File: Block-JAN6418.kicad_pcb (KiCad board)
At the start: 2 copper layers, 48 x 63 mm, 23 parts, among them U1 JAN6418, U2 LM317L

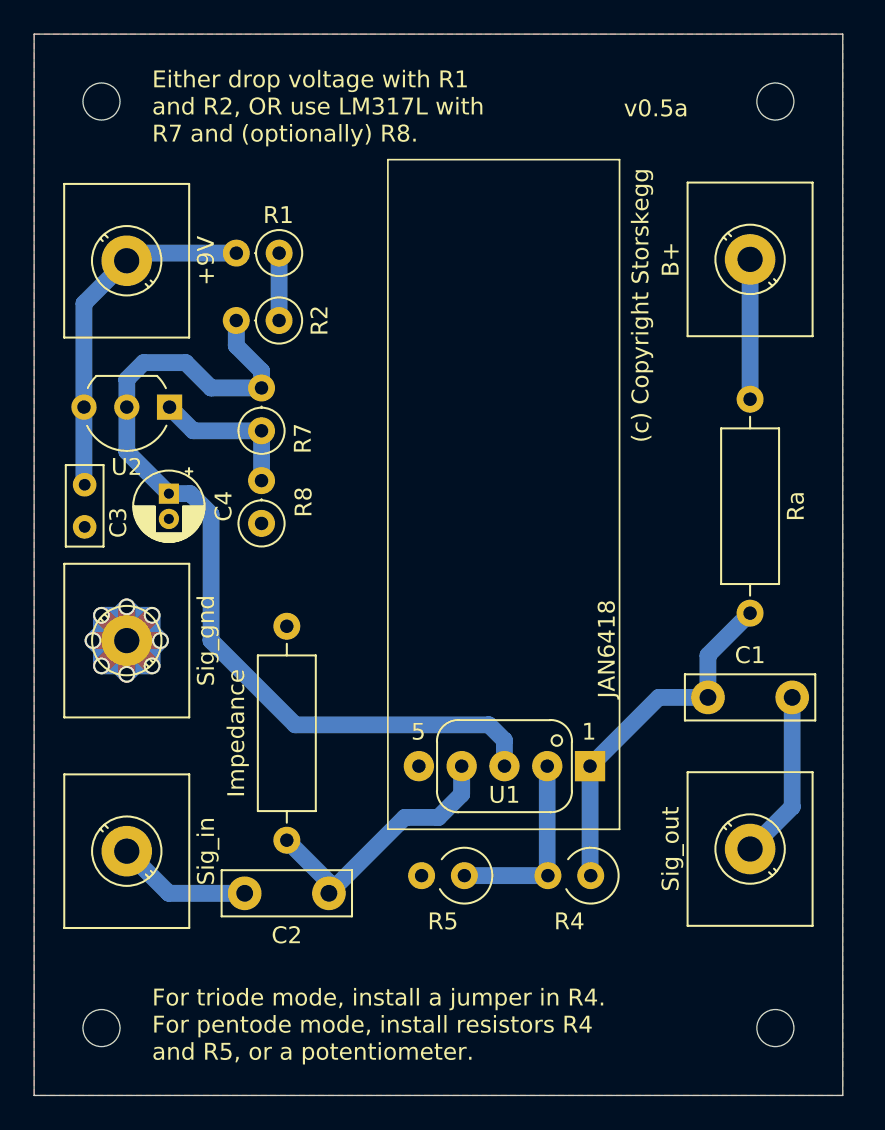
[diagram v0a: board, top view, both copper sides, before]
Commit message: v1.0b Re-routing
- Added ground fill to L2, respective vias
- Re-routed power rail solder points to the bottom of the board so that
  power can be jumpered up from the enclosure front board (will house
  power bars, I/O, pots, etc)
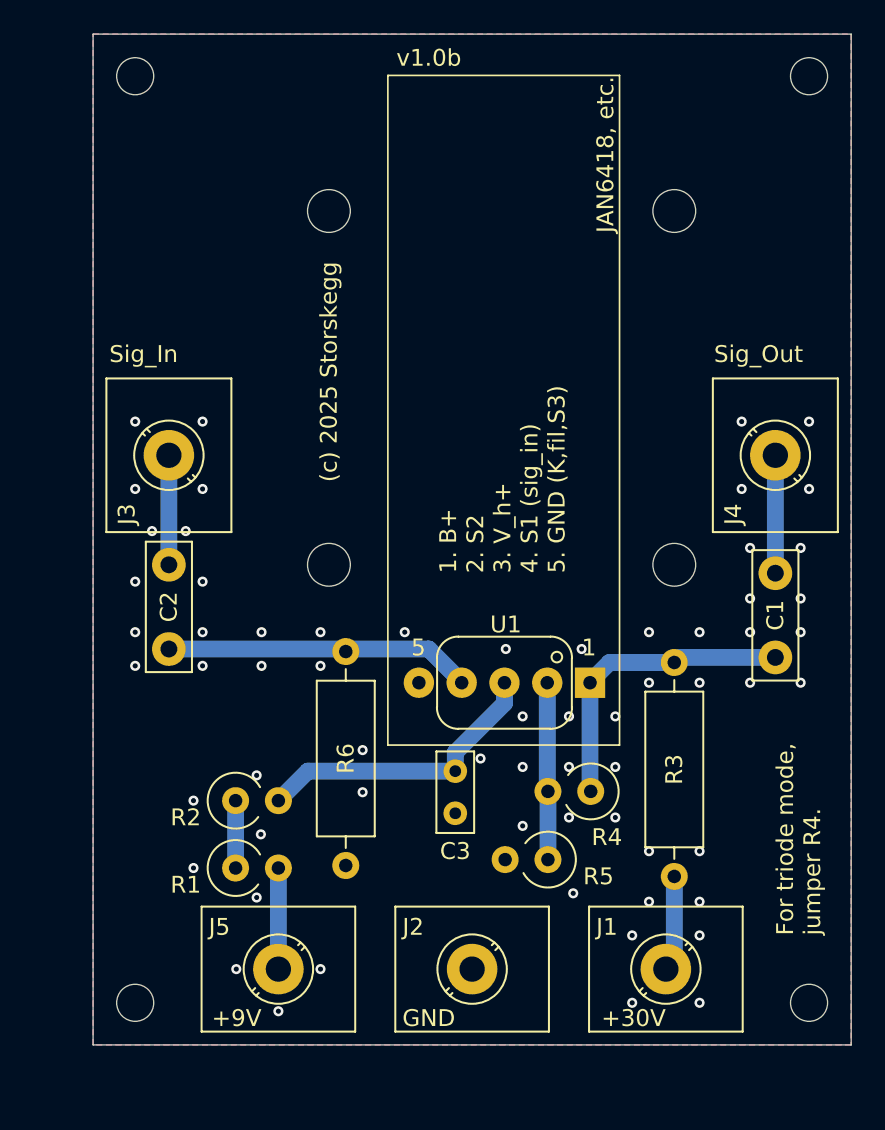
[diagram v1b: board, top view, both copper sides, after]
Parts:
- removed +9V: 9V, TerminalBlock_MetzConnect:TerminalBlock_MetzConnect_360271_1x01_Horizontal_ScrewM3.0_Boxed
- removed B+: B+, TerminalBlock_MetzConnect:TerminalBlock_MetzConnect_360271_1x01_Horizontal_ScrewM3.0_Boxed
- removed C4: 1uF, Capacitor_THT:CP_Radial_D4.0mm_P1.50mm
- removed Impedance: 1M, Resistor_THT:R_Axial_DIN0309_L9.0mm_D3.2mm_P12.70mm_Horizontal
- removed R7: R_r1, Resistor_THT:R_Axial_DIN0207_L6.3mm_D2.5mm_P2.54mm_Vertical
- removed R8: R_r2, Resistor_THT:R_Axial_DIN0207_L6.3mm_D2.5mm_P2.54mm_Vertical
- removed REF** (x4): MountingHole_2.2mm_M2, MountingHole:MountingHole_2.2mm_M2
- removed Ra: Ra, Resistor_THT:R_Axial_DIN0309_L9.0mm_D3.2mm_P12.70mm_Horizontal
- removed Sig_gnd: Sig_gnd, TerminalBlock_MetzConnect:TerminalBlock_MetzConnect_360271_1x01_Horizontal_ScrewM3.0_Boxed
- removed Sig_in: Sig_in, TerminalBlock_MetzConnect:TerminalBlock_MetzConnect_360271_1x01_Horizontal_ScrewM3.0_Boxed
- removed Sig_out: Sig_out, TerminalBlock_MetzConnect:TerminalBlock_MetzConnect_360271_1x01_Horizontal_ScrewM3.0_Boxed
- removed U2: LM317L, Package_TO_SOT_THT:TO-92_Inline_Wide
- added H1: MountingHole, MountingHole:MountingHole_2.2mm_M2, F.Cu at (56.0, 37.5)
- added H2: MountingHole, MountingHole:MountingHole_2.2mm_M2, F.Cu at (96.0, 37.5)
- added H3: MountingHole, MountingHole:MountingHole_2.2mm_M2, F.Cu at (96.0, 92.5)
- added H4: MountingHole, MountingHole:MountingHole_2.2mm_M2, F.Cu at (56.0, 92.5)
- added J1: B+, TerminalBlock_MetzConnect:TerminalBlock_MetzConnect_360271_1x01_Horizontal_ScrewM3.0_Boxed, F.Cu at (87.5, 90.5)
- added J2: Sig_gnd, TerminalBlock_MetzConnect:TerminalBlock_MetzConnect_360271_1x01_Horizontal_ScrewM3.0_Boxed, F.Cu at (76.0, 90.5)
- added J3: Sig_in, TerminalBlock_MetzConnect:TerminalBlock_MetzConnect_360271_1x01_Horizontal_ScrewM3.0_Boxed, F.Cu at (58.0, 60.0)
- added J4: Sig_out, TerminalBlock_MetzConnect:TerminalBlock_MetzConnect_360271_1x01_Horizontal_ScrewM3.0_Boxed, F.Cu at (94.0, 60.0)
- added J5: 9V, TerminalBlock_MetzConnect:TerminalBlock_MetzConnect_360271_1x01_Horizontal_ScrewM3.0_Boxed, F.Cu at (64.5, 90.5)
- added R3: Ra, Resistor_THT:R_Axial_DIN0309_L9.0mm_D3.2mm_P12.70mm_Horizontal, F.Cu at (88.0, 85.0)
- added R6: 1M, Resistor_THT:R_Axial_DIN0309_L9.0mm_D3.2mm_P12.70mm_Horizontal, F.Cu at (68.5, 71.7)
- R1, R2: footprint Resistor_THT:R_Axial_DIN0207_L6.3mm_D2.5mm_P2.54mm_Vertical -> Resistor_THT:R_Axial_DIN0309_L9.0mm_D3.2mm_P2.54mm_Vertical
- moved R1 36.6 mm to (62.0, 84.5), turned to 0 degrees
- moved R2 28.6 mm to (62.0, 80.5), turned to 0 degrees
- moved C3 27.8 mm to (75.0, 78.8)
- moved C2 20.0 mm to (58.0, 66.5), turned to -90 degrees
- moved R5 5.05 mm to (80.5, 84.0)
- moved R4 5.00 mm to (83.0, 80.0)
- moved U1 4.95 mm to (83.0, 73.5)
- moved C1 4.65 mm to (94.0, 72.0), turned to 90 degrees
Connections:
- C3 pad 1: +9V -> Net-(C3-Pad1)
- R2 pad 2: Net-(U2-VO) -> Net-(C3-Pad1)
- U1 pad 3: Net-(U2-VO) -> Net-(C3-Pad1)
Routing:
- net Net-(U2-VO): track 53.4 -> 0.00 mm
- net GND: track 30.1 -> 0.00 mm, vias 8 -> 64
- net Net-(C3-Pad1): track 0.00 -> 17.7 mm
- net +9V: track 20.4 -> 6.00 mm
- net Net-(U2-ADJ): track 9.00 -> 0.00 mm
- net Net-(J1-Pin_1): track 8.30 -> 5.15 mm
- net Net-(U1A-P): track 21.2 -> 18.1 mm
- net Net-(J4-Pin_1): track 10.0 -> 7.00 mm
- net Net-(U1A-G1): track 16.2 -> 18.2 mm
- net Net-(J3-Pin_1): track 8.04 -> 6.50 mm
- net Net-(U1A-G2): track 11.4 -> 10.5 mm
- added copper zone on B.Cu, net GND
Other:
- board size 48 x 63 mm -> 45 x 60 mm
- board text added: "(c) 2025 Storskegg"
- board text added: "+30V"
- board text added: "+9V"
- board text added: "1. B+ 2. S2 3. V_h+ 4. S1 (sig_in) 5. GND (K,fil,S3)"
- board text added: "For triode mode, jumper R4."
- board text added: "GND"
- board text added: "JAN6418, etc."
- board text added: "Sig_In"
- board text added: "Sig_Out"
- board text added: "v1.0b"
- board text removed: "(c) Copyright Storskegg"
- board text removed: "Either drop voltage with R1 and R2, OR use LM317L with R7 and (optionally) R8."
- board text removed: "For triode mode, install a jumper in R4. For pentode mode, install resistors R4 and R5, or a potentiometer."
- board text removed: "JAN6418"
- board text removed: "v0.5a"

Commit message: tighten up some alignments
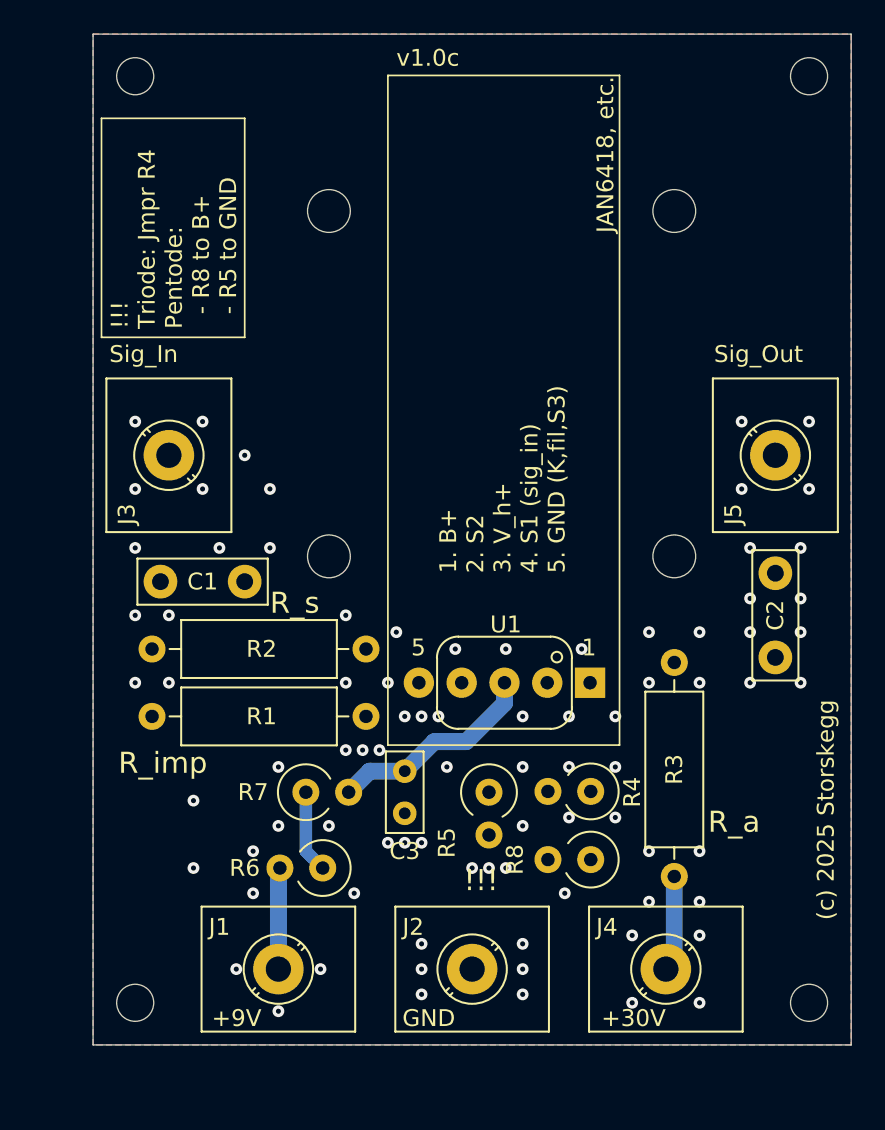
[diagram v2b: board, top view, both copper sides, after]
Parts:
- added R7: R_FilB, Resistor_THT:R_Axial_DIN0309_L9.0mm_D3.2mm_P2.54mm_Vertical, F.Cu at (66.1, 80.0)
- added R8: R_Pent_B+, Resistor_THT:R_Axial_DIN0309_L9.0mm_D3.2mm_P2.54mm_Vertical, F.Cu at (83.0, 84.0)
- J1: value B+ -> 9V
- J4: value Sig_out -> B+
- J5: value 9V -> Sig_out
- R1: value R_FilA -> 1M; footprint Resistor_THT:R_Axial_DIN0309_L9.0mm_D3.2mm_P2.54mm_Vertical -> Resistor_THT:R_Axial_DIN0309_L9.0mm_D3.2mm_P12.70mm_Horizontal
- R2: value R_FilB -> R; footprint Resistor_THT:R_Axial_DIN0309_L9.0mm_D3.2mm_P2.54mm_Vertical -> Resistor_THT:R_Axial_DIN0309_L9.0mm_D3.2mm_P12.70mm_Horizontal
- R4: value R_TriPenA -> R_Tri_Jmpr
- R5: value R_PenB -> R_Pent_gnd
- R6: value 1M -> R_FilA; footprint Resistor_THT:R_Axial_DIN0309_L9.0mm_D3.2mm_P12.70mm_Horizontal -> Resistor_THT:R_Axial_DIN0309_L9.0mm_D3.2mm_P2.54mm_Vertical
- moved J5 42.4 mm to (94.0, 60.0), turned to -90 degrees
- moved C2 36.4 mm to (94.0, 72.0), turned to 90 degrees
- moved C1 31.8 mm to (62.5, 67.5), turned to 180 degrees
- moved J4 31.2 mm to (87.5, 90.5), turned to 0 degrees
- moved J1 23.0 mm to (64.5, 90.5)
- moved R6 12.9 mm to (67.1, 84.5), turned to 180 degrees
- moved R1 10.3 mm to (57.0, 75.5)
- moved R2 10.3 mm to (57.0, 71.5)
- moved R5 5.32 mm to (77.0, 80.0), turned to -90 degrees
- moved C3 3.00 mm to (72.0, 78.8)
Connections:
- C1 pad 1: Net-(U1A-P) -> Net-(J3-Pin_1)
- C1 pad 2: Net-(J4-Pin_1) -> Net-(C1-Pad2)
- C2 pad 1: Net-(J3-Pin_1) -> Net-(U1A-P)
- C2 pad 2: Net-(U1A-G1) -> Net-(J5-Pin_1)
- J1 pad 1: Net-(J1-Pin_1) -> +9V
- J5 pad 1: +9V -> Net-(J5-Pin_1)
- R1 pad 1: Net-(R1-Pad1) -> Net-(C1-Pad2)
- R1 pad 2: +9V -> GND
- R2 pad 1: Net-(R1-Pad1) -> Net-(C1-Pad2)
- R2 pad 2: Net-(C3-Pad1) -> Net-(U1A-G1)
- R3 pad 1: Net-(J1-Pin_1) -> Net-(J4-Pin_1)
- R6 pad 1: Net-(U1A-G1) -> Net-(R6-Pad1)
- R6 pad 2: GND -> +9V
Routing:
- net Net-(U1A-G1): track 18.2 -> 6.49 mm
- net Net-(C1-Pad2): track 0.00 -> 7.50 mm
- net Net-(J5-Pin_1): track 0.00 -> 7.00 mm
- net Net-(J1-Pin_1): track 5.15 -> 0.00 mm
- net Net-(C3-Pad1): track 17.7 -> 12.7 mm
- net Net-(R6-Pad1): track 0.00 -> 4.91 mm
- net Net-(J3-Pin_1): track 6.50 -> 10.6 mm
- net Net-(R1-Pad1): track 4.00 -> 0.00 mm
- net Net-(J4-Pin_1): track 7.00 -> 10.5 mm
- net Net-(U1A-G2): track 10.5 -> 14.0 mm
- net GND: vias 64 -> 84
- added copper zone on In2.Cu, net GND
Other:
- outline, holes or cut-outs redrawn
- copper layers 2 -> 4
- board text added: "!!!"
- board text added: "!!! Triode: Jmpr R4 Pentode: - R8 to B+ - R5 to GND"
- board text added: "R_a"
- board text added: "R_imp"
- board text added: "R_s"
- board text added: "v1.0c"
- board text removed: "For triode mode, jumper R4."
- board text removed: "v1.0b"
